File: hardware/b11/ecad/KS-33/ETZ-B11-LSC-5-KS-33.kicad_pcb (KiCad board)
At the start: 2 copper layers, 112.3 x 85.8 mm, 36 parts, among them SW1 KS-2P02B01-01-a, SW10 KS-2P02B01-01-a, SW11 KS-2P02B01-01-a, SW12 KS-2P02B01-01-a, SW13 KS-2P02B01-01-a, SW14 KS-2P02B01-01-a, SW15 KS-2P02B01-01-a, SW16 KS-2P02B01-01-a, SW17 KS-2P02B01-01-a, SW18 KS-2P02B01-01-a, SW2 KS-2P02B01-01-a, SW3 KS-2P02B01-01-a, SW4 KS-2P02B01-01-a, SW5 KS-2P02B01-01-a, SW6 KS-2P02B01-01-a, SW7 KS-2P02B01-01-a, SW8 KS-2P02B01-01-a, SW9 KS-2P02B01-01-a

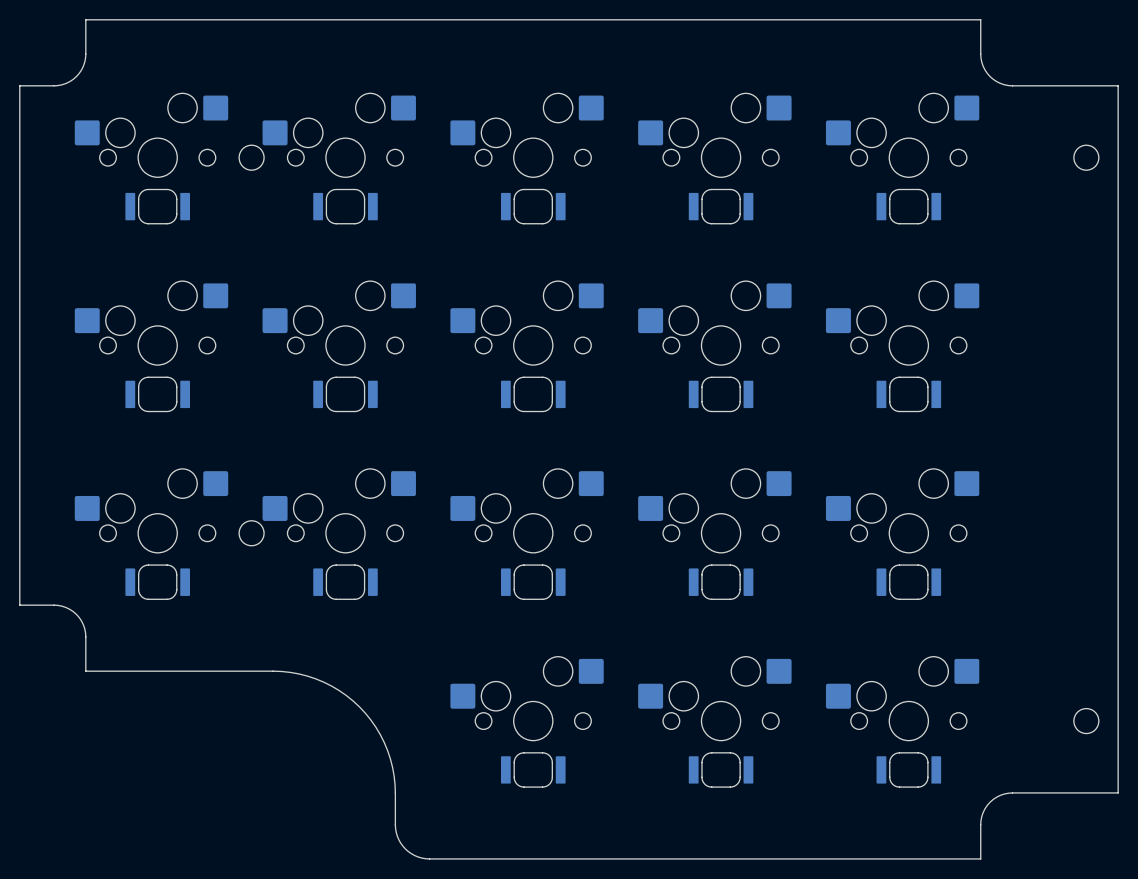
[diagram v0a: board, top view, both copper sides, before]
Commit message: Regenerate B11 PCBs after library cleanup [skip ci]
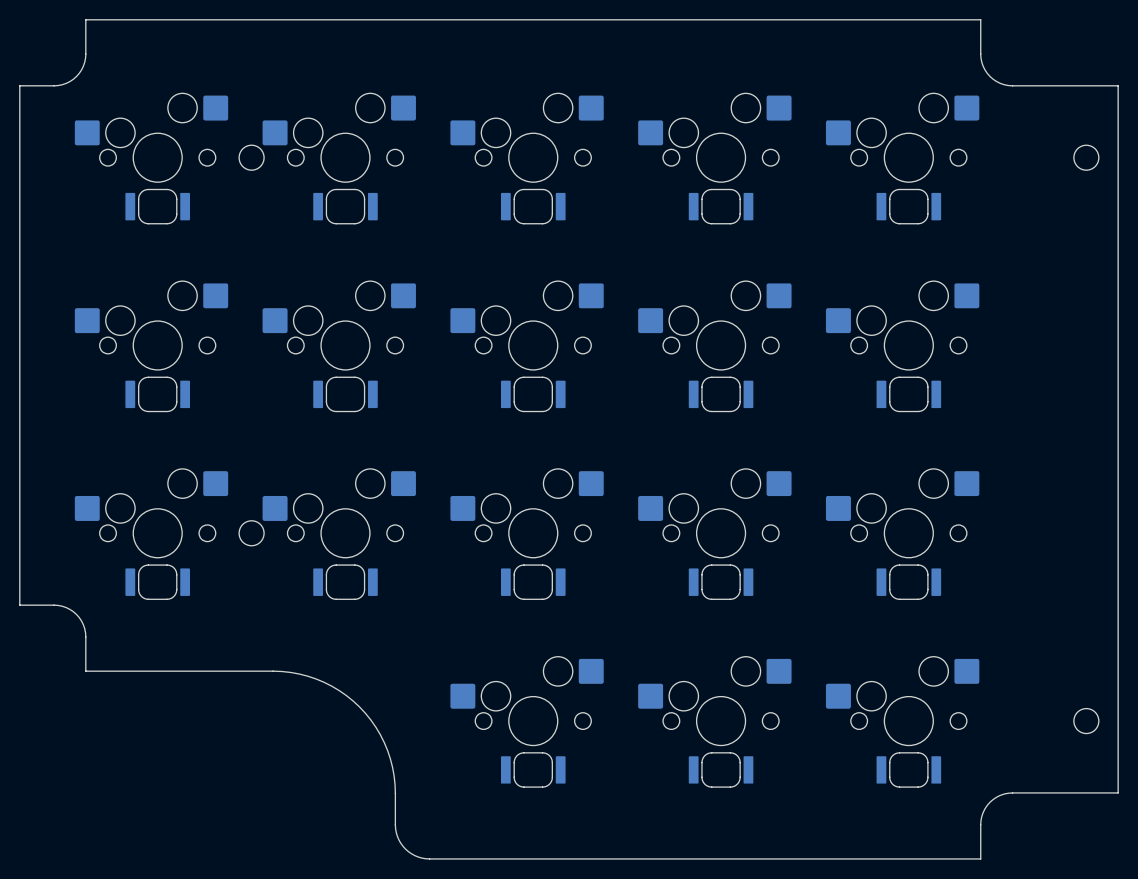
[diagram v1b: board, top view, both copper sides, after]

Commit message: feat: add B11 switch plate schematic foundation (#58)
Signed-off-by: Nikola Secerovski <secersh@gmail.com>
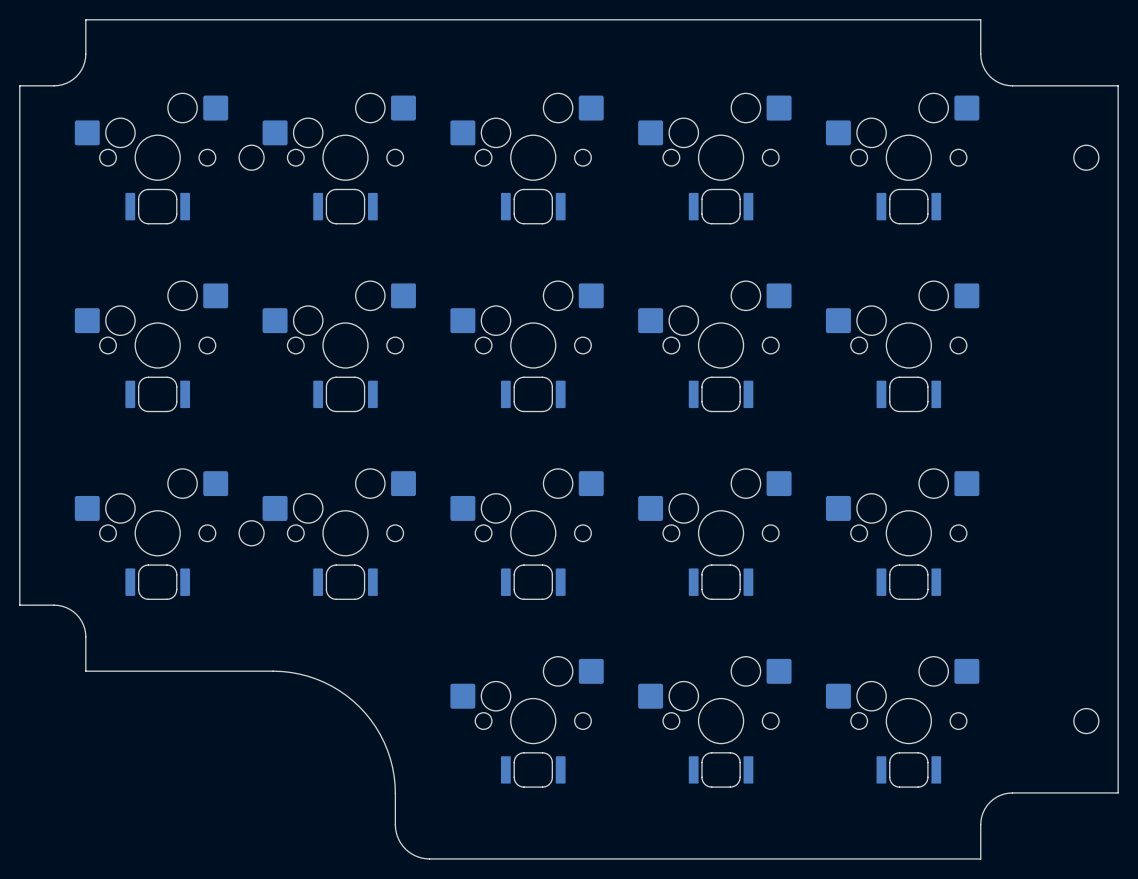
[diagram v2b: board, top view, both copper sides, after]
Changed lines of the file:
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@@
 		(pad "" np_thru_hole circle
 			(at 0 0)
-			(size 5 5)
-			(drill 5)
+			(size 4.6 4.6)
+			(drill 4.6)
 			(layers "*.Cu" "*.Mask")
 		)
@@
 		(pad "" np_thru_hole circle
 			(at 0 0)
-			(size 5 5)
-			(drill 5)
+			(size 4.6 4.6)
+			(drill 4.6)
 			(layers "*.Cu" "*.Mask")
 		)
@@
 		(pad "" np_thru_hole circle
 			(at 0 0)
-			(size 5 5)
-			(drill 5)
+			(size 4.6 4.6)
+			(drill 4.6)
 			(layers "*.Cu" "*.Mask")
 		)
@@
 		(pad "" np_thru_hole circle
 			(at 0 0)
-			(size 5 5)
-			(drill 5)
+			(size 4.6 4.6)
+			(drill 4.6)
 			(layers "*.Cu" "*.Mask")
 		)
@@
 		(pad "" np_thru_hole circle
 			(at 0 0)
-			(size 5 5)
-			(drill 5)
+			(size 4.6 4.6)
+			(drill 4.6)
 			(layers "*.Cu" "*.Mask")
 		)
@@
 		(pad "" np_thru_hole circle
 			(at 0 0)
-			(size 5 5)
-			(drill 5)
+			(size 4.6 4.6)
+			(drill 4.6)
 			(layers "*.Cu" "*.Mask")
 		)
@@
 		(pad "" np_thru_hole circle
 			(at 0 0)
-			(size 5 5)
-			(drill 5)
+			(size 4.6 4.6)
+			(drill 4.6)
 			(layers "*.Cu" "*.Mask")
 		)
@@
 		(pad "" np_thru_hole circle
 			(at 0 0)
-			(size 5 5)
-			(drill 5)
+			(size 4.6 4.6)
+			(drill 4.6)
 			(layers "*.Cu" "*.Mask")
 		)
@@
 		(pad "" np_thru_hole circle
 			(at 0 0)
-			(size 5 5)
-			(drill 5)
+			(size 4.6 4.6)
+			(drill 4.6)
 			(layers "*.Cu" "*.Mask")
 		)
@@
 		(pad "" np_thru_hole circle
 			(at 0 0)
-			(size 5 5)
-			(drill 5)
+			(size 4.6 4.6)
+			(drill 4.6)
 			(layers "*.Cu" "*.Mask")
 		)
@@
 		(pad "" np_thru_hole circle
 			(at 0 0)
-			(size 5 5)
-			(drill 5)
+			(size 4.6 4.6)
+			(drill 4.6)
 			(layers "*.Cu" "*.Mask")
 		)
@@
 		(pad "" np_thru_hole circle
 			(at 0 0)
-			(size 5 5)
-			(drill 5)
+			(size 4.6 4.6)
+			(drill 4.6)
 			(layers "*.Cu" "*.Mask")
 		)
@@
 		(pad "" np_thru_hole circle
 			(at 0 0)
-			(size 5 5)
-			(drill 5)
+			(size 4.6 4.6)
+			(drill 4.6)
 			(layers "*.Cu" "*.Mask")
 		)
@@
 		(pad "" np_thru_hole circle
 			(at 0 0)
-			(size 5 5)
-			(drill 5)
+			(size 4.6 4.6)
+			(drill 4.6)
 			(layers "*.Cu" "*.Mask")
 		)
@@
 		(pad "" np_thru_hole circle
 			(at 0 0)
-			(size 5 5)
-			(drill 5)
+			(size 4.6 4.6)
+			(drill 4.6)
 			(layers "*.Cu" "*.Mask")
 		)
@@
 		(pad "" np_thru_hole circle
 			(at 0 0)
-			(size 5 5)
-			(drill 5)
+			(size 4.6 4.6)
+			(drill 4.6)
 			(layers "*.Cu" "*.Mask")
 		)
@@
 		(pad "" np_thru_hole circle
 			(at 0 0)
-			(size 5 5)
-			(drill 5)
+			(size 4.6 4.6)
+			(drill 4.6)
 			(layers "*.Cu" "*.Mask")
 		)
@@
 		(pad "" np_thru_hole circle
 			(at 0 0)
-			(size 5 5)
-			(drill 5)
+			(size 4.6 4.6)
+			(drill 4.6)
 			(layers "*.Cu" "*.Mask")
 		)
